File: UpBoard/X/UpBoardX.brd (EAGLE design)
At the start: 100 x 80 mm, 120 parts, among them CN1 100nF, CN2 100nF, CN3 100nF, CN4 100nF, IC1 SAM3X8E(ARDUINO), IC2 MEGA16U2-MU, J1 2POSTERMINALBLOCK.25"PITCH, Q1 FDS5680, Q2 FDS5680, Q3 FDS5680, Q4 FDS5680, Q5 SSMJ328R,LF, Q6 2N7002E, Q8 2N7002E, X1 COMS, X2 COMS, X3 GP, X4 CTRL/PYRO, Y1 FH1200001, Y2 ABS05, Y3 406C35D16M00000

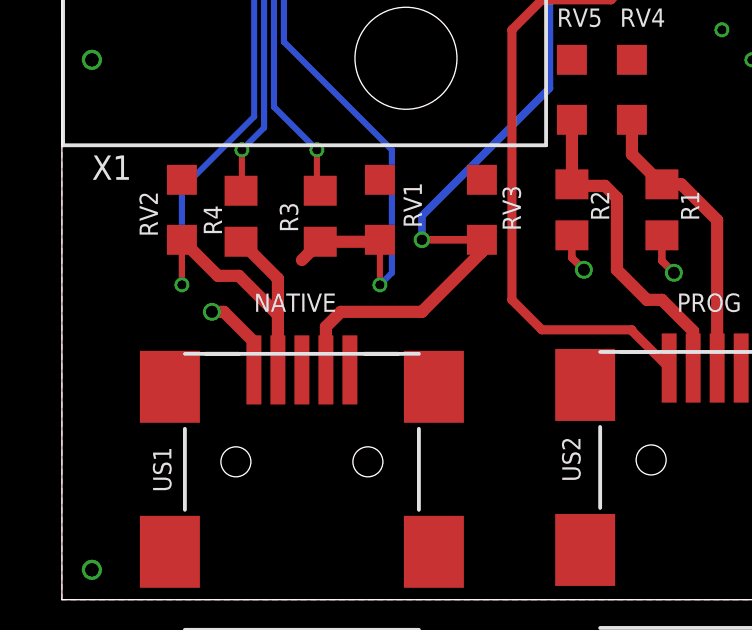
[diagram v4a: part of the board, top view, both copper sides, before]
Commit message: First fixes, schematic appearance changes
Connected D+ line on native USB port. Added title block and reorganized
schematic to fit on a size C sheet. Revision number is now 1.
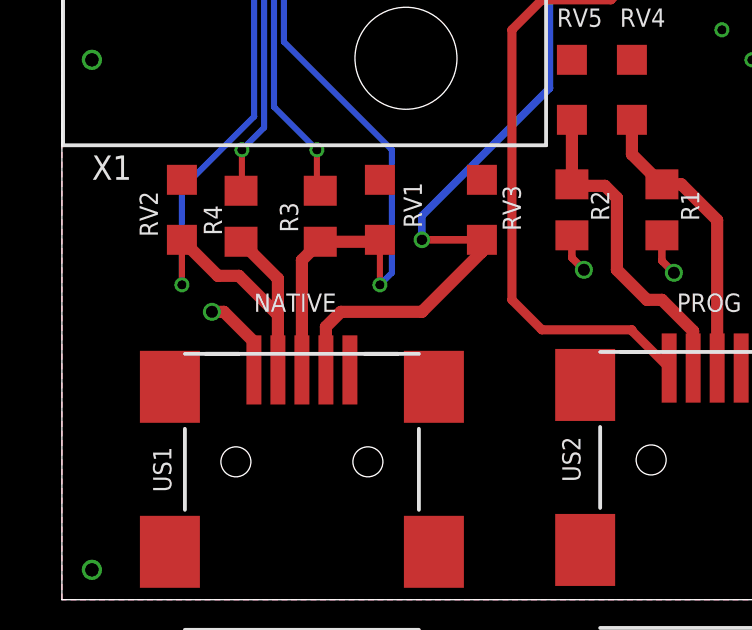
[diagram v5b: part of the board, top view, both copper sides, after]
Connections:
- net D+: now also US1.D+
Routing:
- net D+: track 79.4 -> 83.0 mm
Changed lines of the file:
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@@
 <wire x1="10.6" y1="10.496" x2="10.6" y2="11.831240625" width="0.2032" layer="1"/>
 <wire x1="10.6" y1="11.831240625" x2="10.5" y2="11.931240625" width="0.2032" layer="1"/>
+<contactref element="US1" pad="D+"/>
+<wire x1="8" y1="11.3203625" x2="8" y2="7.66" width="0.4064" layer="1"/>
 </signal>
 <signal name="N$2">

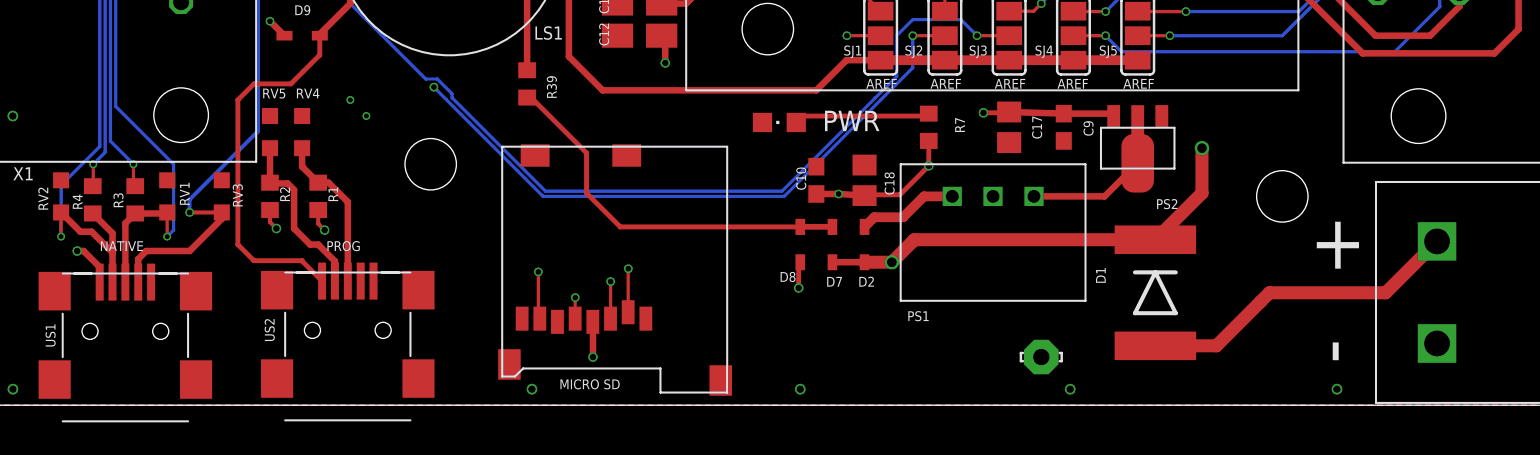
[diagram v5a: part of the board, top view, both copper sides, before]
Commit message: Organized power supply into own module
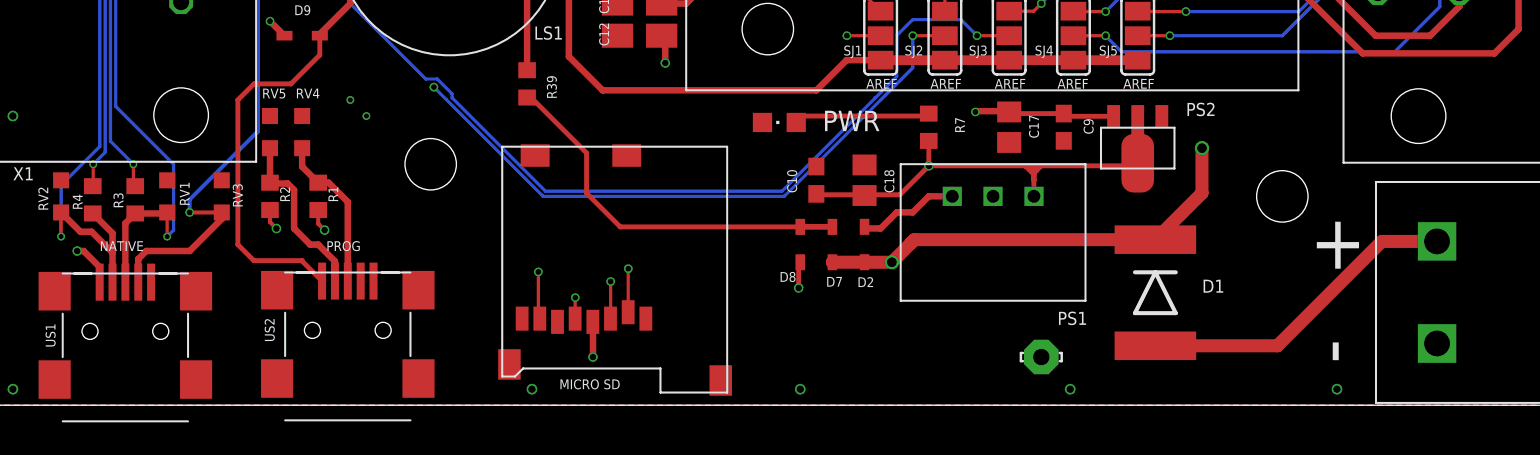
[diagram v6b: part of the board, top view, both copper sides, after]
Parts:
- removed C10, C9: 100nF, resistor:C0603
- removed C17, C18: 100uF, resistor:C0805
- removed D1: S10M-TP, UpBoard:DO-214AB
- removed D2: (no value), zetex:SOD323
- removed PS1: R-78B3.3-1.5, UpBoard B:R-78B3.3-1.5
- removed PS2: AZ1117C, UpBoard B:SOT89
- added PS1-1:C10, PS1-1:C9: 100nF, resistor:C0603
- added PS1-1:C17, PS1-1:C18: 100uF, resistor:C0805
- added PS1-1:D1: S10M-TP, UpBoard:DO-214AB
- added PS1-1:D2: (no value), zetex:SOD323
- added PS1-1:PS1: R-78B3.3-1.5, UpBoard B:R-78B3.3-1.5
- added PS1-1:PS2: AZ1117C, UpBoard B:SOT89
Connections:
- removed net VIN: D1.+, J1.P$1
- new net PS1-1:N$7: PS1-1:D2.1, PS1-1:PS1.1
- net 12V: now also PS1-1:D1.-, PS1-1:D2.2; no longer D1.-, D2.2
- net 3.3V: now also PS1-1:C10.1, PS1-1:C18.1, PS1-1:PS1.3, PS1-1:PS2.2, PS1-1:PS2.2@1; no longer C10.1, C18.1, PS1.3, PS2.2, PS2.2@1
- net 5V: now also PS1-1:C17.1, PS1-1:C9.1, PS1-1:PS2.3; no longer C17.1, C9.1, PS2.3
- net GND: now also PS1-1:C10.2, PS1-1:C17.2, PS1-1:C18.2, PS1-1:C9.2, PS1-1:PS1.2, PS1-1:PS2.1; no longer C10.2, C17.2, C18.2, C9.2, PS1.2, PS2.1
- net N$7: now also J1.P$1, PS1-1:D1.+; no longer D2.1, PS1.1
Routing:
- net VIN: track 20.3 -> 0.00 mm
- net N$7: track 6.25 -> 20.2 mm
- net 3.3V: track 132.3 -> 142.1 mm, vias 22 -> 21
- net PS1-1:N$7: track 0.00 -> 6.33 mm
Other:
- board text added: "C10"
- board text added: "C17"
- board text added: "C18"
- board text added: "C9"
- board text added: "D1"
- board text added: "D2"
- board text added: "PS1"
- board text added: "PS2"

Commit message: Sheet Changes
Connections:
- net N$7 renamed VIN
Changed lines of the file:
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@@
 <wire x1="54.1" y1="11" x2="54" y2="11.1" width="0.4064" layer="1"/>
 </signal>
-<signal name="N$7">
+<signal name="VIN">
 <contactref element="J1" pad="P$1"/>
 <contactref element="PS1-1:D1" pad="+"/>
